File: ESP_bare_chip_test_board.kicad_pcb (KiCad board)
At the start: 4 copper layers, 57.1 x 63.5 mm, 86 parts, among them J1201 NorComp - 112-024-113RYY1, J1301 Conn_01x06, J1302 Conn_01x06, J1501 Conn_01x04, J1502 Conn_01x04, J201 Conn_01x06, J501 Barrel_Jack, J502 PWR_IN, J503 ALTERNATE, J801 USB_C_Receptacle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

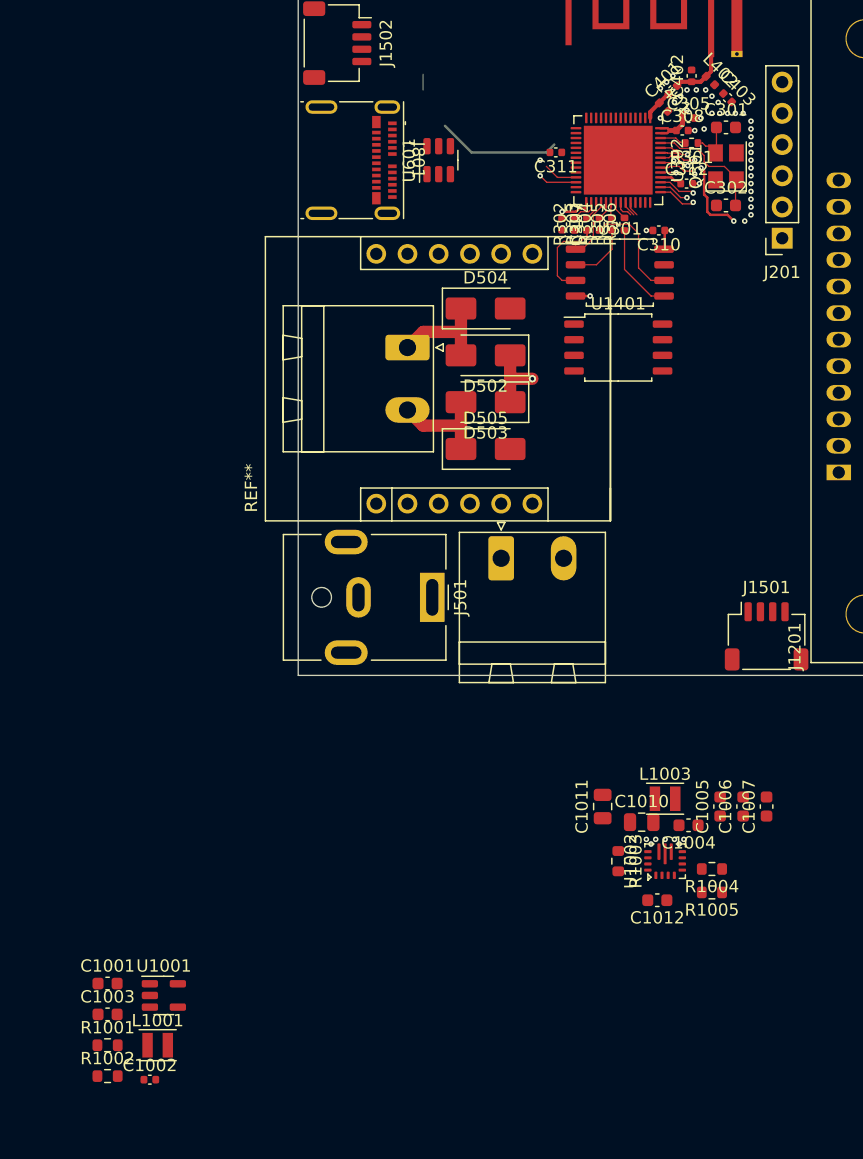
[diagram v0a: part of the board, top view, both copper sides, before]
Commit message: Layed-out 5V buck-boost regulator ciruit
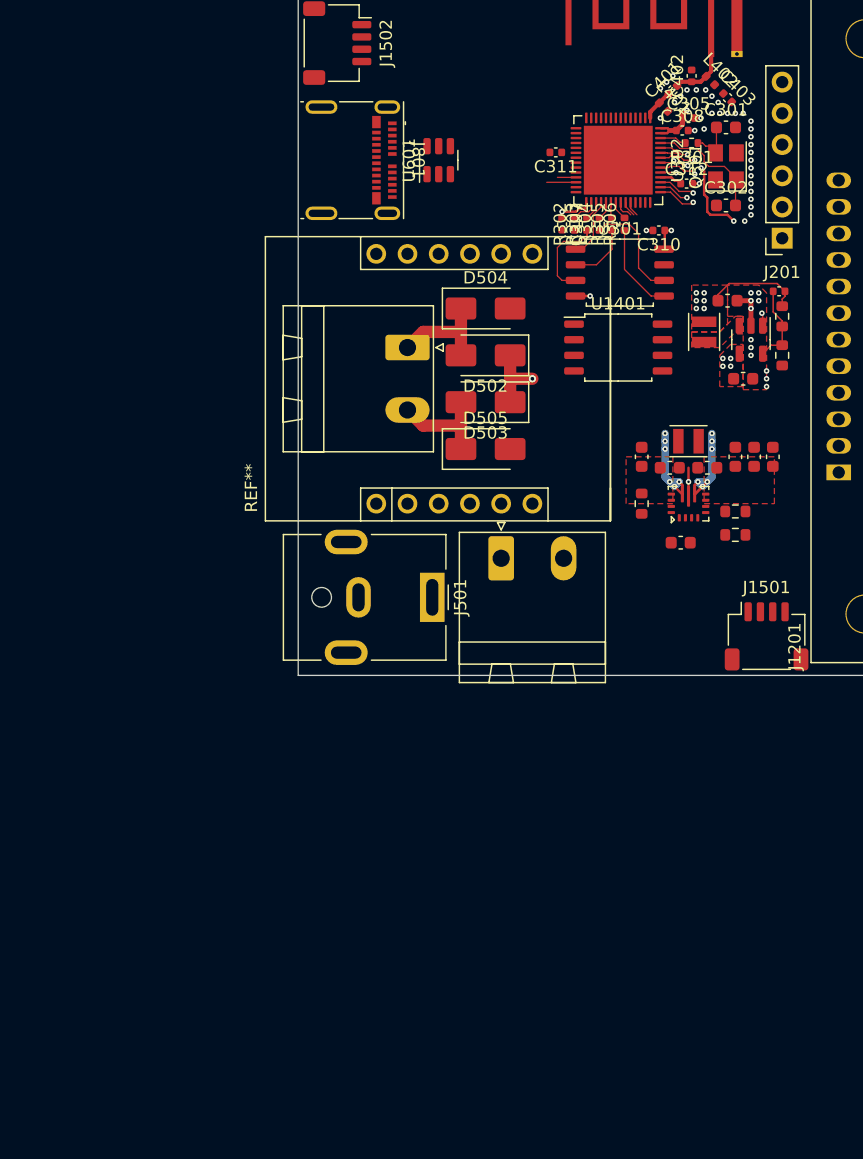
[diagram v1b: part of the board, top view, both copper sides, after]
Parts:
- C1010, C1011: footprint Capacitor_SMD:C_0805_2012Metric -> Capacitor_SMD:C_0603_1608Metric
- moved C1002 82.0 mm to (153.4, 79.2), turned to 180 degrees
- moved R1001 80.8 mm to (153.7, 81.3), turned to -90 degrees
- moved R1002 80.3 mm to (153.7, 84.5), turned to -90 degrees
- moved C1003 76.9 mm to (149.2, 80.0)
- moved L1001 73.1 mm to (147.3, 82.5), turned to 90 degrees
- moved U1001 71.6 mm to (151.1, 83.2), turned to -90 degrees
- moved C1001 71.4 mm to (150.5, 86.4)
- moved C1012 29.1 mm to (145.4, 99.7)
- moved L1003 29.1 mm to (146.1, 91.4)
- moved R1003 29.1 mm to (142.2, 96.5)
- moved R1004 29.1 mm to (149.9, 97.2)
- moved R1005 29.1 mm to (149.9, 99.1)
- moved U1002 29.1 mm to (146.1, 96.5)
- moved C1004 29.1 mm to (147.6, 93.6)
- moved C1010 28.9 mm to (144.5, 93.6)
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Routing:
- net /ESP32-S3/ESP32-S3-core/VDD_SPI: track 15.2 -> 5.16 mm
- net /Power/buck-boost-5v/L2: track 0.00 -> 9.37 mm, vias 0 -> 6
- net /Power/buck-boost-5v/L1: track 0.00 -> 7.95 mm, vias 0 -> 6
- net +3V3: track 6.07 -> 13.9 mm, vias 1 -> 7
- net +5V: track 0.00 -> 7.61 mm, vias 0 -> 5
- net /Power/step-down-5v-3v3_ESP32/FB: track 0.00 -> 6.56 mm
- net GND: track 9.60 -> 15.1 mm, vias 35 -> 47
- net /USB_D+: track 4.40 -> 2.38 mm, vias 2 -> 0
- net /USB_D-: track 2.79 -> 1.51 mm
- net (no net): vias 10 -> 3
- added copper zone on F.Cu, net +3V3
- added copper zone on F.Cu, net +5V
- added copper zone on F.Cu, net /Power/V_{IN}
- added copper zone on F.Cu, net /Power/step-down-5v-3v3_ESP32/SW

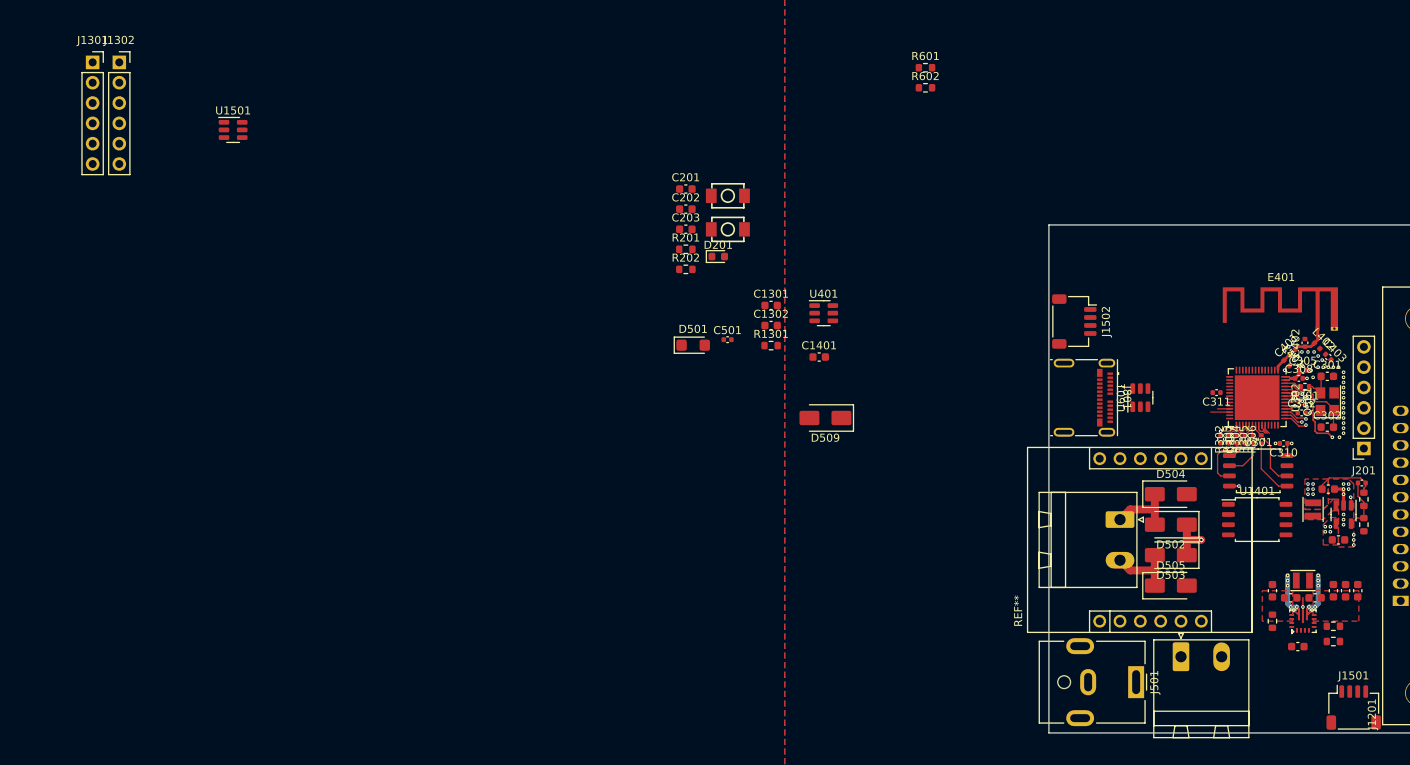
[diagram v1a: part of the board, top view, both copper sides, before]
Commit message: Planning/wiring up some traces on PCB
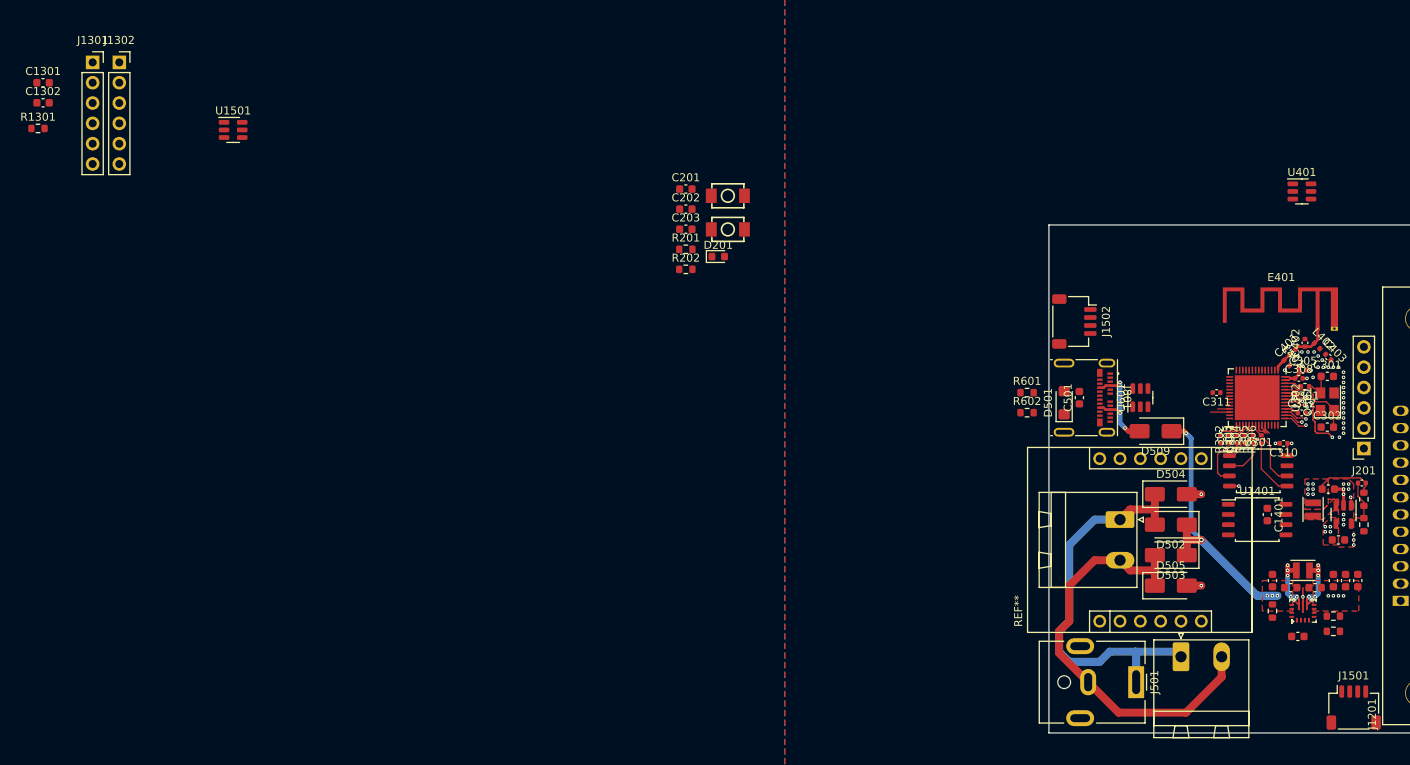
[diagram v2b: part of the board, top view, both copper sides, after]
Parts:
- C501: value 1uF/25V -> 10uF/25v; footprint Capacitor_SMD:C_0402_1005Metric -> Capacitor_SMD:C_0603_1608Metric
- moved R1301 95.6 mm to (-12.1, 34.9)
- moved C1301 95.2 mm to (-11.4, 29.2)
- moved C1302 95.2 mm to (-11.4, 31.7)
- moved U401 61.7 mm to (145.9, 42.8)
- moved C1401 59.4 mm to (141.6, 83.2), turned to -90 degrees
- moved D501 46.9 mm to (116.2, 69.2), turned to 90 degrees
- moved C501 44.6 mm to (118.1, 68.6), turned to 90 degrees
- moved R602 42.5 mm to (111.6, 70.5)
- moved R601 42.5 mm to (111.6, 67.9)
- moved D509 41.3 mm to (127.6, 72.8)
- moved C1004 1.27 mm to (147.6, 92.3)
- moved C1010 1.27 mm to (144.5, 92.3)
- moved C1005 1.27 mm to (149.9, 91.4)
- moved C1006 1.27 mm to (151.4, 91.4)
- moved C1007 1.27 mm to (152.9, 91.4)
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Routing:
- net /Power/V_{IN}_Right: track 8.69 -> 53.1 mm
- net /Power/V_{IN}_Left: track 8.69 -> 50.6 mm
- net /Power/V_{IN}: track 5.62 -> 34.1 mm, vias 1 -> 5
- net /Power/VBUS: track 0.00 -> 13.5 mm, vias 0 -> 3
- net +5V: track 7.61 -> 1.05 mm, vias 5 -> 9
- net GND: track 15.1 -> 18.7 mm, vias 47 -> 49
- net /Power/buck-boost-5v/L2: track 9.37 -> 10.4 mm
- net /Power/buck-boost-5v/L1: track 7.95 -> 9.03 mm
- added copper zone on In2.Cu, net +3V3
- added copper zone on In2.Cu, net +5V

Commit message: Picked part numbers and placed most remaining MCU support components
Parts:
- added C303: 10uF/10V, Capacitor_SMD:C_0603_1608Metric, F.Cu at (137.3, 62.0)
- added C304: 1uF, Capacitor_SMD:C_0402_1005Metric, F.Cu at (139.3, 62.2)
- added C306: 0.1uF, Capacitor_SMD:C_0402_1005Metric, F.Cu at (140.3, 62.2)
- added C309: 0.1uF, Capacitor_SMD:C_0402_1005Metric, F.Cu at (142.4, 63.4)
- added L301: 2.0nH(0.1nH), Inductor_SMD:L_0402_1005Metric, F.Cu at (141.4, 62.5)
- R301: value TBD, 24nH to start -> 24nH
- moved C203 81.8 mm to (146.7, 72.9), turned to -90 degrees
- moved C201 67.4 mm to (133.3, 62.2), turned to 90 degrees
- moved R201 66.2 mm to (133.3, 65.4), turned to 90 degrees
- moved SW202 58.7 mm to (130.8, 62.9), turned to -90 degrees
- moved SW201 55.7 mm to (126.4, 62.9), turned to -90 degrees
- moved R202 52.2 mm to (120.0, 41.9), turned to 180 degrees
- moved D201 51.3 mm to (123.5, 41.9)
- moved C202 47.4 mm to (116.2, 41.3)
- moved C1005 6.63 mm to (143.5, 89.5)
- moved C1011 6.63 mm to (135.9, 89.5)
- moved L1003 6.63 mm to (139.7, 88.3)
- moved R1003 6.63 mm to (135.9, 93.3)
- moved R1004 6.63 mm to (143.5, 94.0)
- moved R1005 6.63 mm to (143.5, 95.9)
- moved U1002 6.63 mm to (139.7, 93.3)
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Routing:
- net +3V3: track 13.9 -> 21.6 mm, vias 7 -> 10
- net /Power/V_{IN}: track 34.1 -> 27.5 mm
- net VDD3P3: track 0.00 -> 3.59 mm
- net /ESP32-S3/ESP_EN: track 0.00 -> 2.05 mm, vias 0 -> 1
- net /ESP32-S3/IO7: track 0.00 -> 1.90 mm, vias 0 -> 1
- net /ESP32-S3/IO1: track 0.00 -> 1.79 mm, vias 0 -> 1
- net /ESP32-S3/IO3: track 0.00 -> 1.77 mm, vias 0 -> 1
- net /ESP32-S3/IO5: track 0.00 -> 1.75 mm, vias 0 -> 1
- net /ESP32-S3/IO8: track 0.00 -> 1.43 mm, vias 0 -> 1
- net /ESP32-S3/IO6: track 0.00 -> 1.34 mm, vias 0 -> 1
- net /ESP32-S3/IO36: track 3.02 -> 1.82 mm, vias 1 -> 0
- net /ESP32-S3/IO4: track 0.00 -> 1.07 mm, vias 0 -> 1
- net /ESP32-S3/IO38: track 4.39 -> 3.45 mm, vias 1 -> 0
- net /ESP32-S3/IO2: track 0.00 -> 0.91 mm, vias 0 -> 1
- net /ESP32-S3/ESP_BOOT: track 0.00 -> 0.89 mm, vias 0 -> 1
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
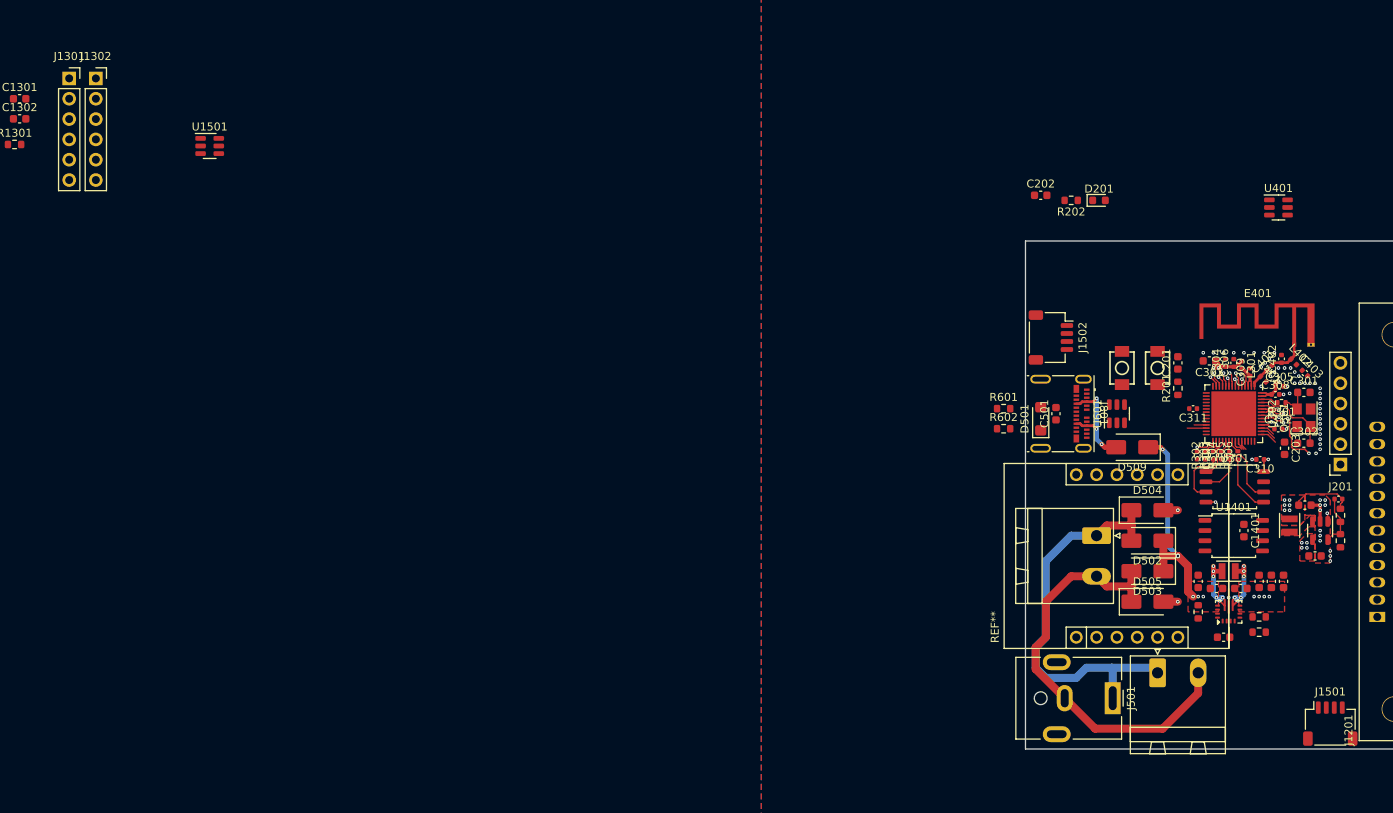
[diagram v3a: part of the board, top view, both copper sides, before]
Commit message: Started wiring up traces
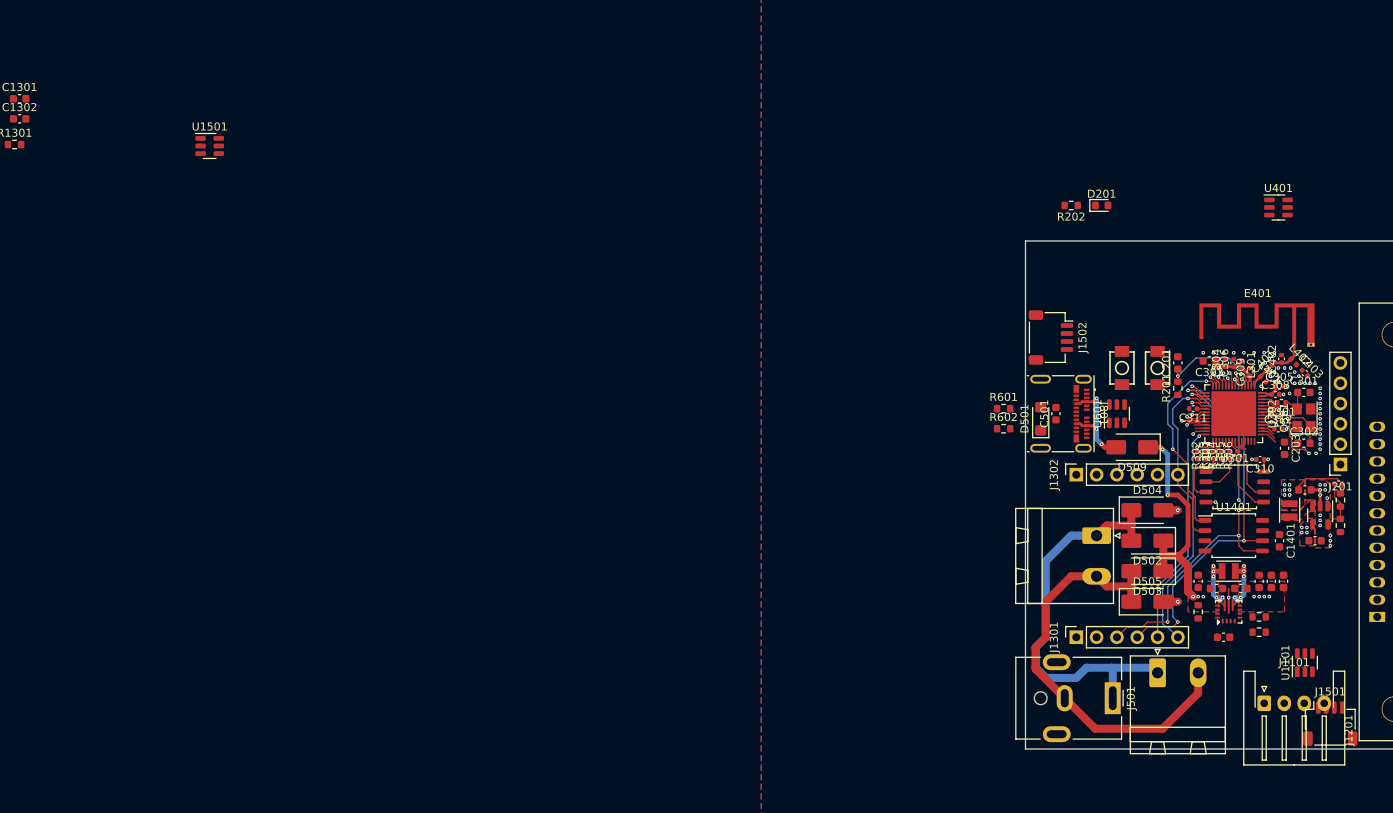
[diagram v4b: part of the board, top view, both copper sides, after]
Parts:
- removed C202: 100nF/50V, Capacitor_SMD:C_0603_1608Metric
- removed REF**: USR-ES1, Module_custom:USR-ES1
- added J1101: Conn_01x04, Connector_JST:JST_XH_S4B-XH-A-1_1x04_P2.50mm_Horizontal, F.Cu at (144.1, 104.8)
- added U1101: D1213A-04TS-7, Package_TO_SOT_SMD:TSOT-23-6, F.Cu at (149.2, 99.7)
- moved J1301 144.0 mm to (120.7, 96.5), turned to 90 degrees
- moved J1302 132.2 mm to (120.7, 76.2), turned to 90 degrees
- moved C1401 4.62 mm to (146.1, 84.5)
- moved C1001 1.91 mm to (150.5, 84.5)
- moved C1002 1.91 mm to (153.4, 77.3)
- moved C1003 1.91 mm to (149.2, 78.1)
- moved L1001 1.91 mm to (147.3, 80.6)
- moved R1001 1.91 mm to (153.7, 79.4)
- moved R1002 1.91 mm to (153.7, 82.5)
- moved U1001 1.91 mm to (151.1, 81.3)
- moved D201 0.72 mm to (123.8, 42.5)
- moved R202 0.64 mm to (120.0, 42.5)
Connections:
- net /ESP32-S3/IO37 renamed /4pin_connector/J0_pin3
- net /ESP32-S3/IO38 renamed /4pin_connector/J0_pin4
- U302 pad 28: /ESP32-S3/IO26 -> /~{ETH_INT}
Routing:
- net /MOSI: track 0.00 -> 52.4 mm, vias 0 -> 4
- net /CLK: track 0.00 -> 47.7 mm, vias 0 -> 4
- net /~{ETH_INT}: track 0.00 -> 28.9 mm, vias 0 -> 1
- net /~{ETH_CS0}: track 0.00 -> 28.5 mm, vias 0 -> 1
- net /~{FRAM_CS}: track 0.00 -> 24.4 mm, vias 0 -> 2
- net /MISO: track 0.00 -> 22.5 mm, vias 0 -> 1
- net /ESP32-S3/ESP_EN: track 2.05 -> 13.6 mm, vias 1 -> 2
- net /ESP32-S3/IO17: track 0.00 -> 3.16 mm, vias 0 -> 1
- net /ESP32-S3/IO16: track 0.00 -> 2.69 mm, vias 0 -> 1
- net /ESP32-S3/IO18: track 0.00 -> 2.57 mm, vias 0 -> 1
- net /ESP32-S3/IO14: track 0.00 -> 1.93 mm, vias 0 -> 1
- net /ESP32-S3/IO15: track 0.00 -> 1.90 mm, vias 0 -> 1
- net /Power/V_{IN}: track 27.5 -> 29.3 mm
- net /ESP32-S3/IO21: track 0.00 -> 1.78 mm, vias 0 -> 1
- net +3V3: track 21.6 -> 22.7 mm
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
